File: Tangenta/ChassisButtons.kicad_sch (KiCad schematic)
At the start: 22 parts, among them J2 Conn_02x02_Top_Bottom, Q1 2N7002, Q2 2N7002, U5 74HC74D,653, U6 CD4060SA_TR, U7 74HC04D,653

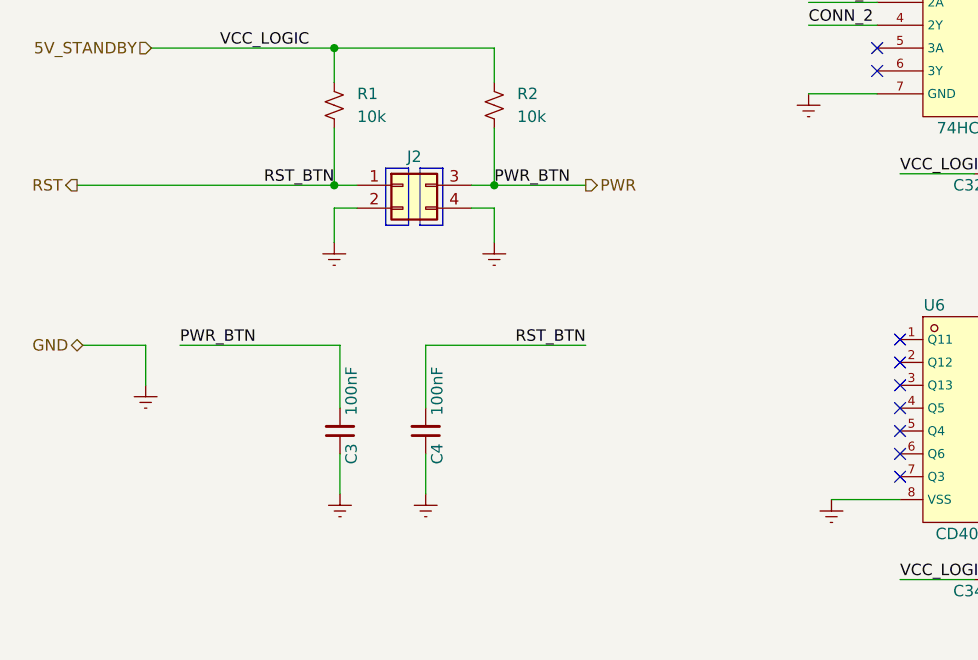
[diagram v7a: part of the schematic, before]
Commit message: Adding on-board PWR and RST tactile buttons.
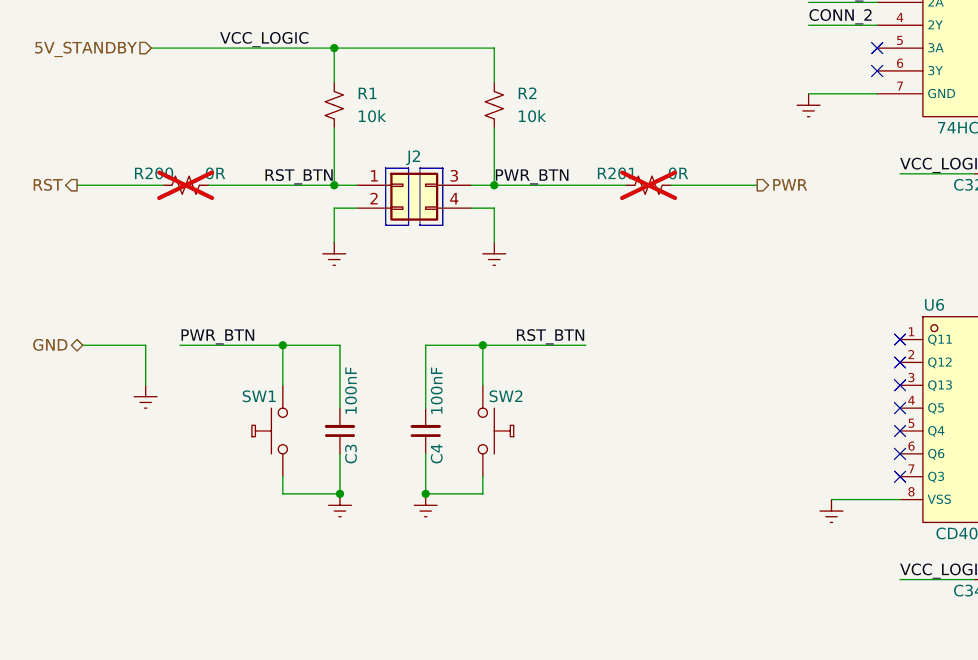
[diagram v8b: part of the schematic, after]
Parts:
- added R200, R201: 0R, Resistor_SMD:R_0603_1608Metric, symbol Device:R_Small_US
- added SW1, SW2: TSC015A04818B, Tactile_BTN:Tactile_BTN, symbol Tactile_BTN:TSC015A04818B
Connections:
- net GNDREF: now also SW1.1, SW2.1
- net PWR: now also R201.2; no longer C3.2, J2.3 (Pin_3), R2.2, U6.12 (MR), U7.1 (1A)
- net RST: now also R200.1; no longer C4.2, J2.1 (Pin_1), R1.2
- new net PWR_BTN: C3.2, J2.3 (Pin_3), R2.2, R201.1, SW1.3, U6.12 (MR), U7.1 (1A)
- new net RST_BTN: C4.2, J2.1 (Pin_1), R1.2, R200.2, SW2.3
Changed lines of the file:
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@@
   (junction (at 68.58 68.58) (diameter 0) (color 0 0 0 0)
   )
+  (junction (at 78.74 118.11) (diameter 0) (color 0 0 0 0)
+  )
+  (junction (at 62.865 101.6) (diameter 0) (color 0 0 0 0)
+  )
+  (junction (at 69.215 118.11) (diameter 0) (color 0 0 0 0)
+  )
+  (junction (at 85.09 101.6) (diameter 0) (color 0 0 0 0)
+  )
   (junction (at 176.53 116.205) (diameter 0) (color 0 0 0 0)
   )
+  (junction (at 86.36 83.82) (diameter 0) (color 0 0 0 0)
+  )
   (junction (at 211.455 121.285) (diameter 0) (color 0 0 0 0)
   )
-  (junction (at 86.36 83.82) (diameter 0) (color 0 0 0 0)
-  )
   (junction (at 226.695 102.235) (diameter 0) (color 0 0 0 0)
   )
+  (junction (at 68.58 83.82) (diameter 0) (color 0 0 0 0)
+  )
   (junction (at 237.49 102.235) (diameter 0) (color 0 0 0 0)
-  )
-  (junction (at 68.58 83.82) (diameter 0) (color 0 0 0 0)
   )
   (no_connect (at 154.305 71.12))
@@
     (stroke (width 0) (type default))
   )
+  (wire (pts (xy 86.36 83.82) (xy 100.965 83.82))
+    (stroke (width 0) (type default))
+  )
   (wire (pts (xy 86.36 72.39) (xy 86.36 68.58))
     (stroke (width 0) (type default))
@@
     (stroke (width 0) (type default))
   )
+  (wire (pts (xy 40.005 83.82) (xy 49.53 83.82))
+    (stroke (width 0) (type default))
+  )
   (wire (pts (xy 68.58 72.39) (xy 68.58 68.58))
     (stroke (width 0) (type default))
   )
+  (wire (pts (xy 106.045 83.82) (xy 115.57 83.82))
+    (stroke (width 0) (type default))
+  )
+  (wire (pts (xy 85.09 116.205) (xy 85.09 118.11))
+    (stroke (width 0) (type default))
+  )
   (wire (pts (xy 226.695 102.235) (xy 237.49 102.235))
     (stroke (width 0) (type default))
   )
-  (wire (pts (xy 96.52 101.6) (xy 78.74 101.6))
+  (wire (pts (xy 96.52 101.6) (xy 85.09 101.6))
     (stroke (width 0) (type default))
   )
@@
     (stroke (width 0) (type default))
   )
+  (wire (pts (xy 54.61 83.82) (xy 68.58 83.82))
+    (stroke (width 0) (type default))
+  )
   (wire (pts (xy 204.47 82.55) (xy 212.725 82.55))
     (stroke (width 0) (type default))
@@
     (stroke (width 0) (type default))
   )
+  (wire (pts (xy 62.865 116.205) (xy 62.865 118.11))
+    (stroke (width 0) (type default))
+  )
   (wire (pts (xy 176.53 111.76) (xy 176.53 116.205))
     (stroke (width 0) (type default))
@@
     (stroke (width 0) (type default))
   )
+  (wire (pts (xy 62.865 118.11) (xy 69.215 118.11))
+    (stroke (width 0) (type default))
+  )
   (wire (pts (xy 194.945 58.42) (xy 202.565 58.42))
     (stroke (width 0) (type default))
@@
     (stroke (width 0) (type default))
   )
+  (wire (pts (xy 62.865 101.6) (xy 62.865 106.045))
+    (stroke (width 0) (type default))
+  )
   (wire (pts (xy 226.695 102.235) (xy 226.695 116.205))
     (stroke (width 0) (type default))
@@
     (stroke (width 0) (type default))
   )
-  (wire (pts (xy 86.36 83.82) (xy 96.52 83.82))
-    (stroke (width 0) (type default))
-  )
   (wire (pts (xy 170.815 111.76) (xy 176.53 111.76))
     (stroke (width 0) (type default))
@@
     (stroke (width 0) (type default))
   )
-  (wire (pts (xy 40.005 83.82) (xy 68.58 83.82))
+  (wire (pts (xy 62.865 101.6) (xy 69.215 101.6))
+    (stroke (width 0) (type default))
+  )
+  (wire (pts (xy 85.09 101.6) (xy 85.09 106.045))
     (stroke (width 0) (type default))
   )
@@
     (stroke (width 0) (type default))
   )
+  (wire (pts (xy 85.09 118.11) (xy 78.74 118.11))
+    (stroke (width 0) (type default))
+  )
   (wire (pts (xy 69.215 101.6) (xy 69.215 108.585))
     (stroke (width 0) (type default))
@@
     (stroke (width 0) (type default))
   )
-  (wire (pts (xy 51.435 101.6) (xy 69.215 101.6))
+  (wire (pts (xy 51.435 101.6) (xy 62.865 101.6))
     (stroke (width 0) (type default))
   )
@@
   )
   (wire (pts (xy 161.925 111.76) (xy 165.735 111.76))
+    (stroke (width 0) (type default))
+  )
+  (wire (pts (xy 85.09 101.6) (xy 78.74 101.6))
     (stroke (width 0) (type default))
   )
@@
     (effects (font (size 1.27 1.27)) (justify left bottom))
   )
-  (hierarchical_label "PWR" (shape output) (at 96.52 83.82 0) (fields_autoplaced)
+  (hierarchical_label "PWR" (shape output) (at 115.57 83.82 0) (fields_autoplaced)
     (effects (font (size 1.27 1.27)) (justify left))
   )
@@
     )
   )
+  (symbol (lib_id "Tactile_BTN:TSC015A04818B") (at 60.833 111.125 90) (unit 1)
+    (in_bom yes) (on_board yes) (dnp no)
+    (property "Reference" "SW1" (at 58.293 107.315 90)
+      (effects (font (size 1.27 1.27)) (justify right))
+    )
+    (property "Value" "TSC015A04818B" (at 64.008 112.395 90)
+      (effects (font (size 1.27 1.27)) (justify right) hide)
+    )
+    (property "Footprint" "Tactile_BTN:Tactile_BTN" (at 71.501 114.554 0)
+      (effects (font (size 1.27 1.27) italic) hide)
+    )
+    (property "Datasheet" "https://item.szlcsc.com/503640.html" (at 73.787 125.603 0)
+      (effects (font (size 1.27 1.27)) (justify left) hide)
+    )
+    (property "LCSC" "C2888508" (at 69.215 120.65 0)
+      (effects (font (size 1.27 1.27)) hide)
+    )
+    (pin "1")
+    (pin "3")
+    (instances
+      (project "Tangenta"
+        (path "/358d1bcf-7599-4352-8c4d-baa18a5f09e6/8215796b-9611-4f43-bcc5-319f8414b8a6"
+          (reference "SW1") (unit 1)
+        )
+      )
+    )
+  )
   (symbol (lib_id "Device:C_Small") (at 215.265 82.55 90) (unit 1)
     (in_bom yes) (on_board yes) (dnp no)
@@
     )
   )
+  (symbol (lib_id "Device:R_Small_US") (at 103.505 83.82 90) (unit 1)
+    (in_bom no) (on_board yes) (dnp yes)
+    (property "Reference" "R201" (at 102.235 82.55 90)
+      (effects (font (size 1.27 1.27)) (justify left))
+    )
+    (property "Value" "0R" (at 107.95 82.55 90)
+      (effects (font (size 1.27 1.27)) (justify left))
+    )
+    (property "Footprint" "Resistor_SMD:R_0603_1608Metric" (at 103.505 83.82 0)
+      (effects (font (size 1.27 1.27)) hide)
+    )
+    (property "Datasheet" "~" (at 103.505 83.82 0)
+      (effects (font (size 1.27 1.27)) hide)
+    )
+    (pin "1")
+    (pin "2")
+    (instances
+      (project "Tangenta"
+        (path "/358d1bcf-7599-4352-8c4d-baa18a5f09e6/8215796b-9611-4f43-bcc5-319f8414b8a6"
+          (reference "R201") (unit 1)
+        )
+      )
+    )
+  )
   (symbol (lib_id "Connector_Generic:Conn_02x02_Top_Bottom") (at 76.2 83.82 0) (unit 1)
     (in_bom yes) (on_board yes) (dnp no)
@@
     )
   )
+  (symbol (lib_id "Device:R_Small_US") (at 52.07 83.82 90) (unit 1)
+    (in_bom no) (on_board yes) (dnp yes)
+    (property "Reference" "R200" (at 50.8 82.55 90)
+      (effects (font (size 1.27 1.27)) (justify left))
+    )
+    (property "Value" "0R" (at 56.515 82.55 90)
+      (effects (font (size 1.27 1.27)) (justify left))
+    )
+    (property "Footprint" "Resistor_SMD:R_0603_1608Metric" (at 52.07 83.82 0)
+      (effects (font (size 1.27 1.27)) hide)
+    )
+    (property "Datasheet" "~" (at 52.07 83.82 0)
+      (effects (font (size 1.27 1.27)) hide)
+    )
+    (pin "1")
+    (pin "2")
+    (instances
+      (project "Tangenta"
+        (path "/358d1bcf-7599-4352-8c4d-baa18a5f09e6/8215796b-9611-4f43-bcc5-319f8414b8a6"
+          (reference "R200") (unit 1)
+        )
+      )
+    )
+  )
   (symbol (lib_id "Device:R_Small_US") (at 241.3 102.235 90) (unit 1)
     (in_bom yes) (on_board yes) (dnp no)
@@
         )
       )
+    )
+  )
+  (symbol (lib_id "Tactile_BTN:TSC015A04818B") (at 87.122 111.125 270) (mirror x) (unit 1)
+    (in_bom yes) (on_board yes) (dnp no)
+    (property "Reference" "SW2" (at 89.662 107.315 90)
+      (effects (font (size 1.27 1.27)) (justify right))
+    )
+    (property "Value" "TSC015A04818B" (at 83.947 112.395 90)
+      (effects (font (size 1.27 1.27)) (justify right) hide)
+    )
+    (property "Footprint" "Tactile_BTN:Tactile_BTN" (at 76.454 114.554 0)
+      (effects (font (size 1.27 1.27) italic) hide)
+    )
+    (property "Datasheet" "https://item.szlcsc.com/503640.html" (at 74.168 125.603 0)
+      (effects (font (size 1.27 1.27)) (justify left) hide)
+    )
+    (property "LCSC" "C2888508" (at 78.74 120.65 0)
+      (effects (font (size 1.27 1.27)) hide)
+    )
+    (pin "1")
+    (pin "3")
+    (instances
+      (project "Tangenta"
+        (path "/358d1bcf-7599-4352-8c4d-baa18a5f09e6/8215796b-9611-4f43-bcc5-319f8414b8a6"
+          (reference "SW2") (unit 1)
+        )
+      )
